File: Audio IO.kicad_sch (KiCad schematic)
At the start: 11 parts, among them J601 DAC1, J611 DAC2, J621 DAC3, J701 ADC1, J702 ADC2

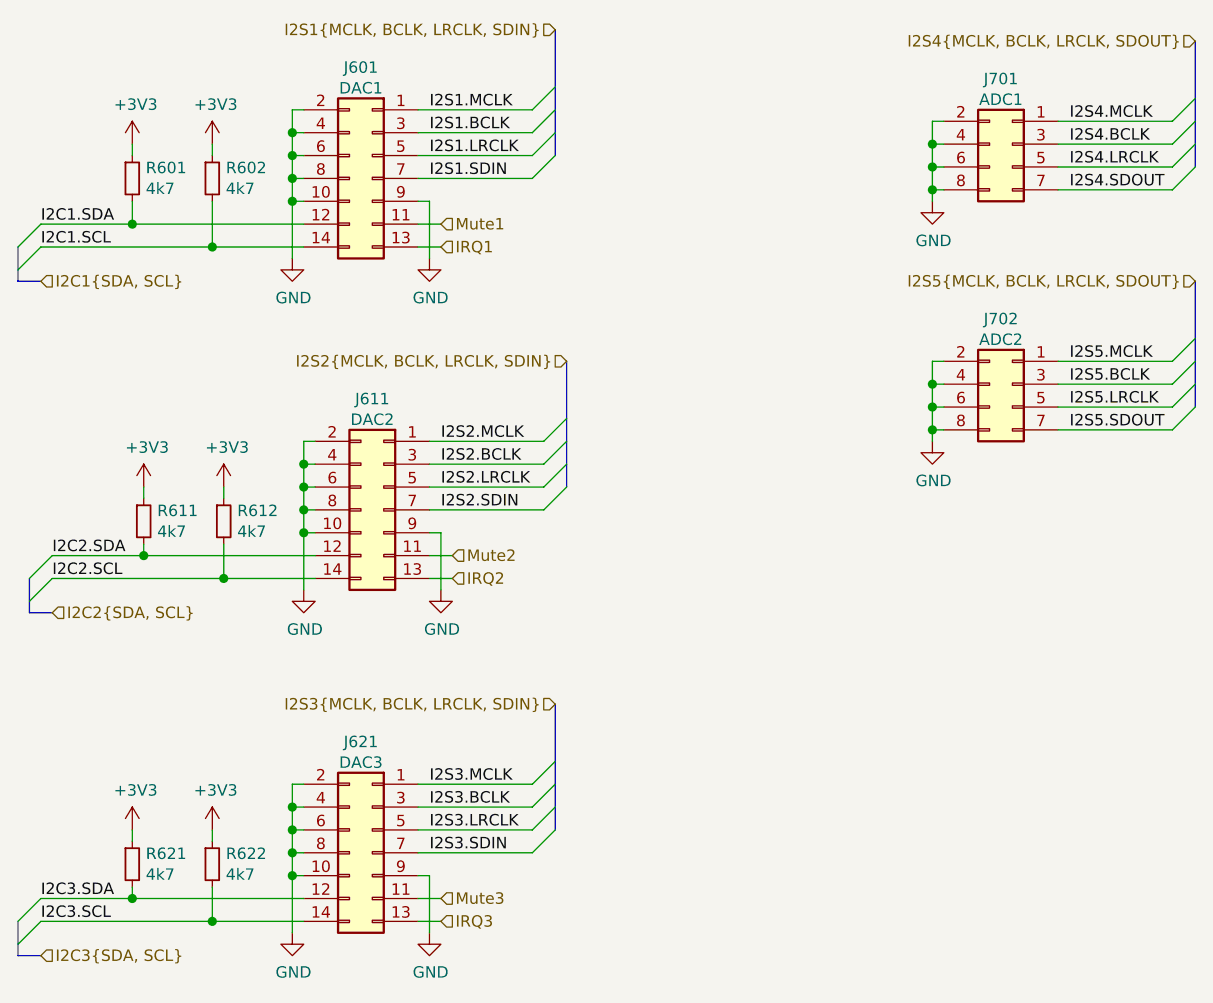
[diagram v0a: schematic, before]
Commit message: Update to KiCad 6
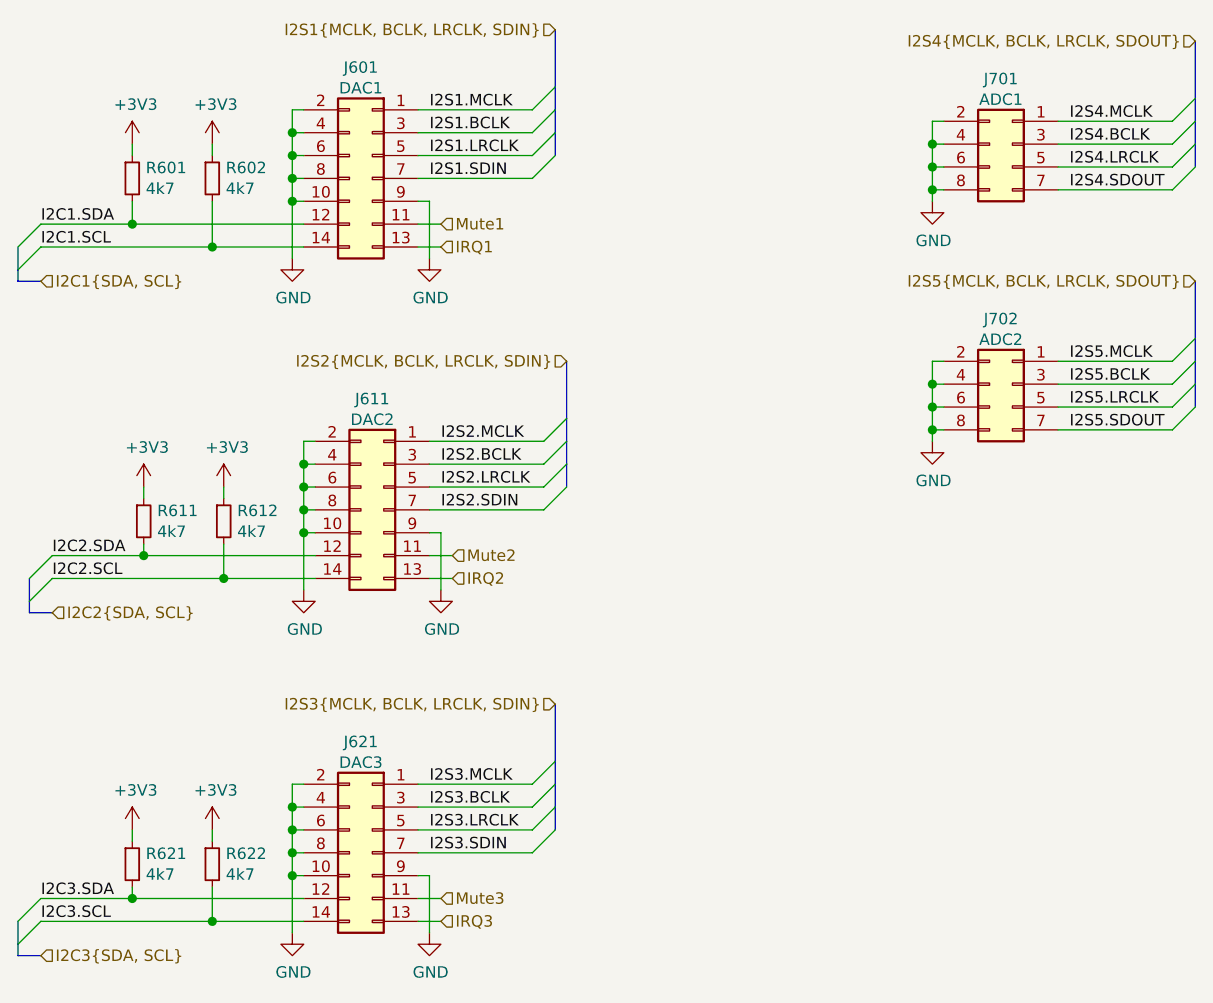
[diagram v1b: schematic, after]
